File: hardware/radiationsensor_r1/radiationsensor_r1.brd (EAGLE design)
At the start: 30 x 46.5 mm, 39 parts, among them CN1 1X09, U1 LMP7721, U2 MAX4477, U4 MAX4477, U5 50k

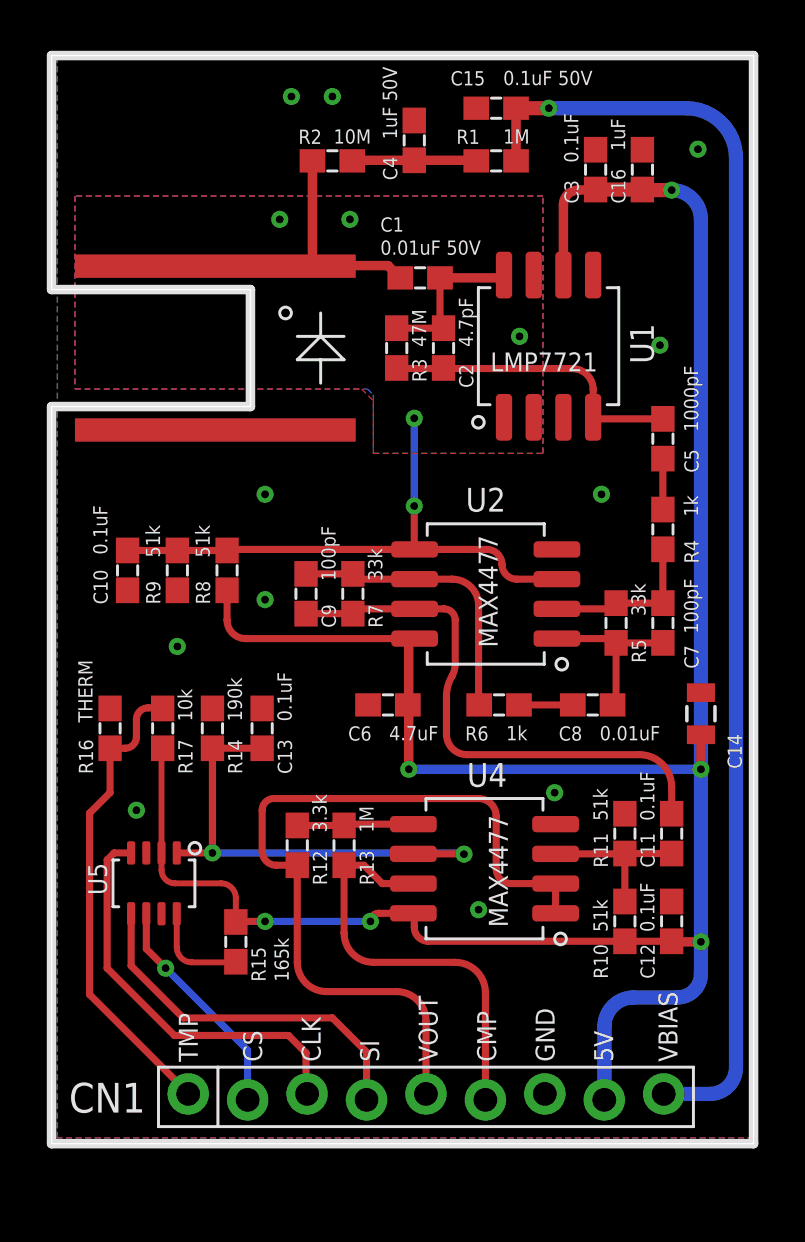
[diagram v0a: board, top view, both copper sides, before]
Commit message: Added shield connection to radiation sensor rev1
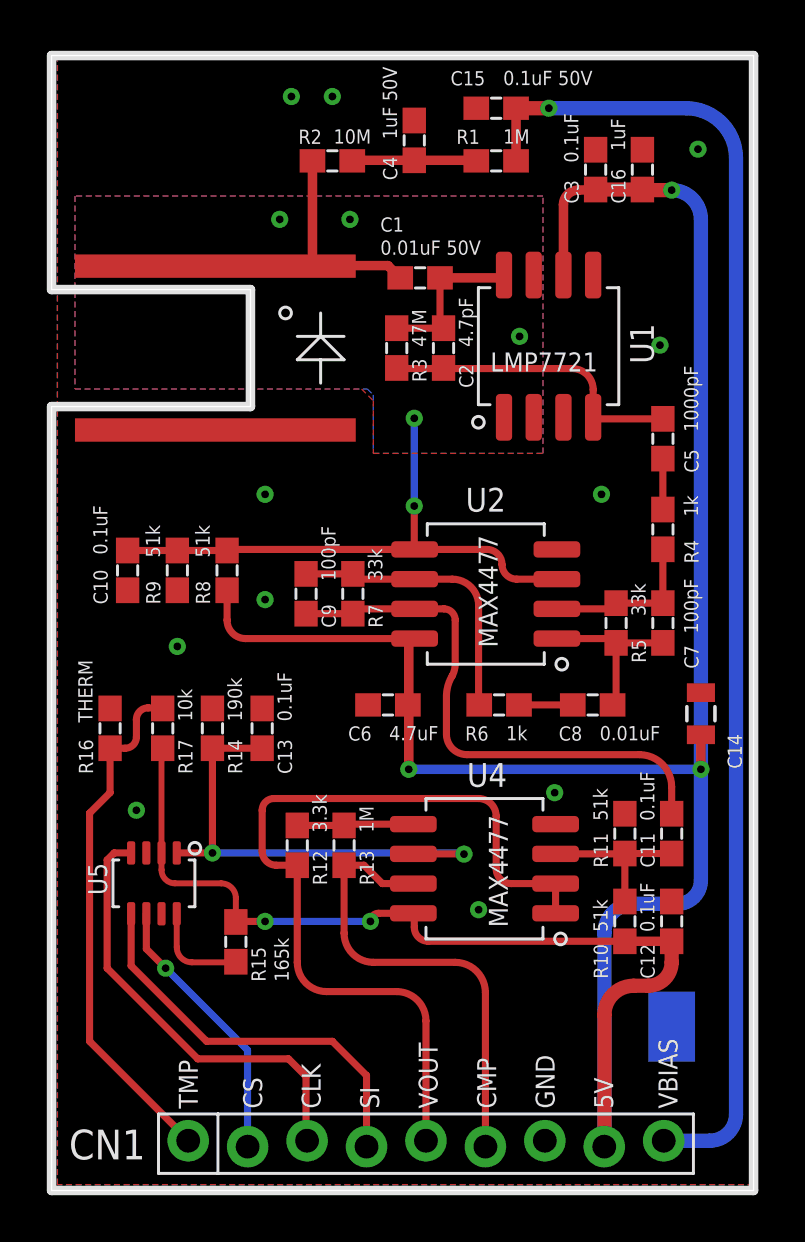
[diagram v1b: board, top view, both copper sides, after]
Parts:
- added CN2: GROUND-PAD, openct:GROUND-PAD
- moved CN1 2.00 mm to (51.0, 21.0)
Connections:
- net GND: now also CN2.GND
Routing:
- net 5V: track 110.8 -> 121.9 mm, vias 6 -> 5
- net VTEMP: track 20.3 -> 22.3 mm
- net VOUT: track 34.1 -> 36.1 mm
- net VBIAS: track 55.0 -> 57.0 mm
- net CS: track 9.75 -> 11.7 mm
- net COMP_OUT: track 17.9 -> 19.9 mm
- net SCLK: track 17.5 -> 19.0 mm
- net MOSI: track 15.9 -> 17.3 mm
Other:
- board size 30 x 46.5 mm -> 30 x 48.5 mm
- board text added: "SHIELD"
